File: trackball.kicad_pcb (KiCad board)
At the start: 2 copper layers, 27.5 x 35.2 mm, 38 parts, among them P1 CONN_10, P2 CONN_5, U1 MKL03Z32VFK4, U2 ADNS-3530, U4 ESD

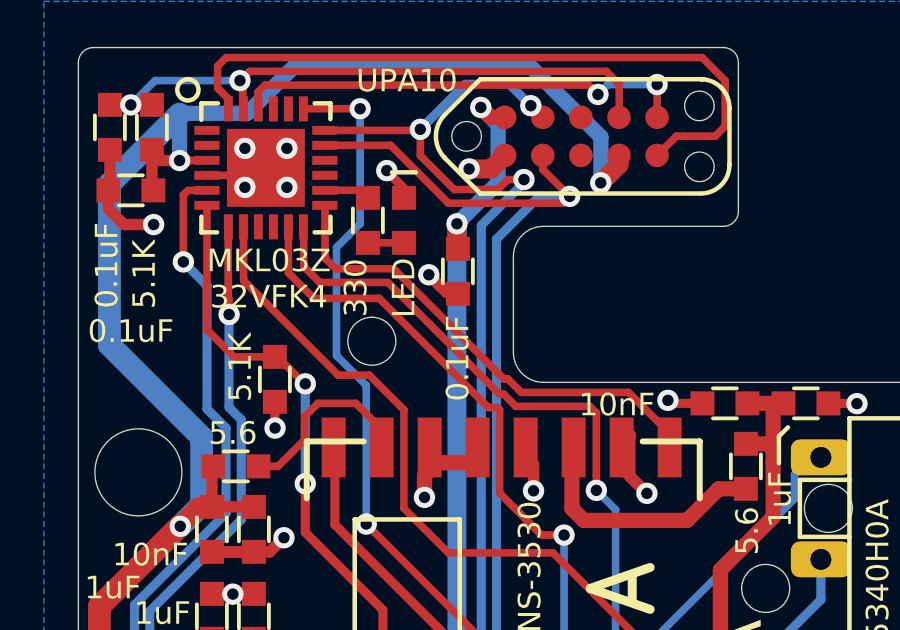
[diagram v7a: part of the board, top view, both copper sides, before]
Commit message: Remove redudant C13.
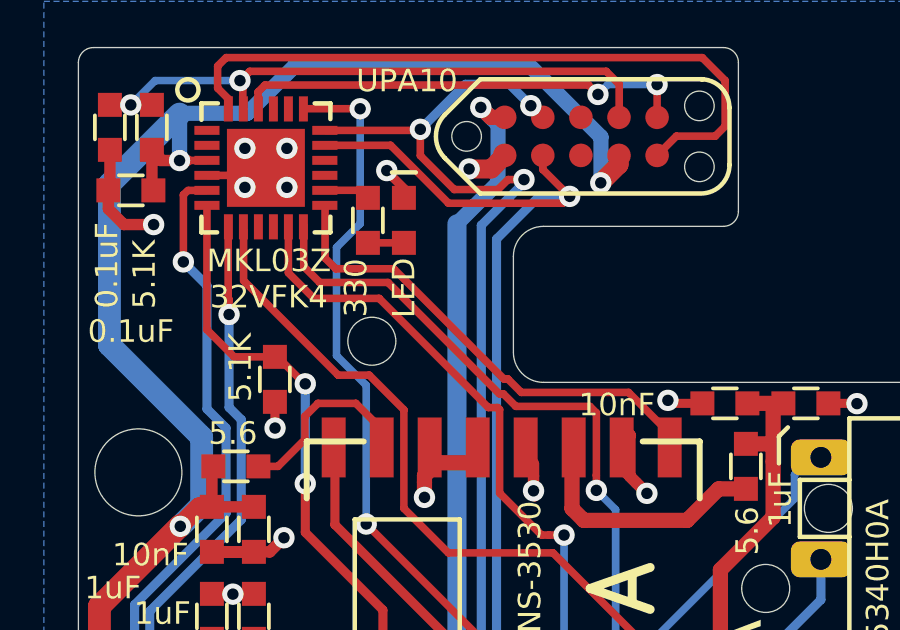
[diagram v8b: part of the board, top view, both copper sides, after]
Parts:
- removed C13: 0.1uF, ugl:SM0603
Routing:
- net GND: track 37.0 -> 35.7 mm, vias 21 -> 20
- net +5V: track 37.6 -> 36.7 mm, vias 3 -> 2
